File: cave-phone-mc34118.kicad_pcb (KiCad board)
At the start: 2 copper layers, 98.7 x 54.2 mm, 71 parts, among them J1 Conn_01x02_Female, SW1 L-KLS7-SK02-12E12-EG7, SW2 SW_SPST, SW3 SW_SPST, T1 SM-LP-5001, U1 LT1935, U2 MC34118, U3 MC34119G-SO8

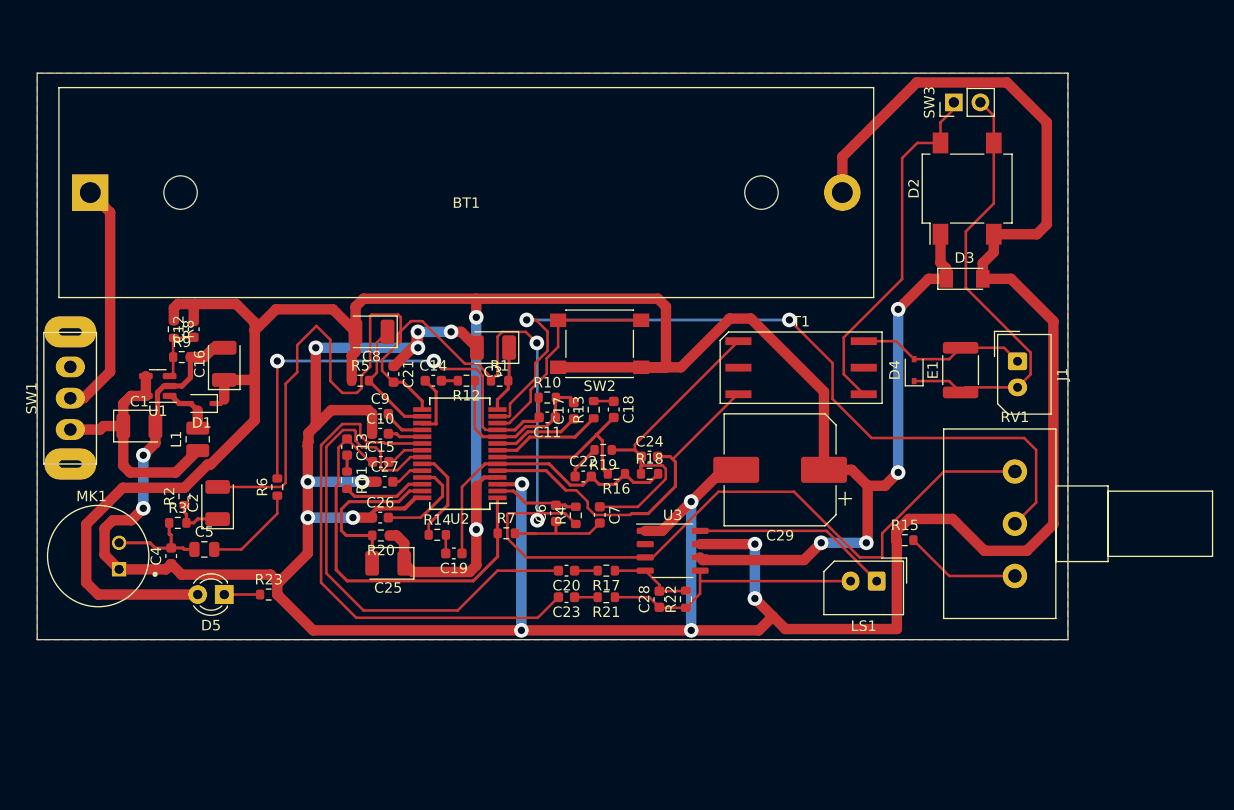
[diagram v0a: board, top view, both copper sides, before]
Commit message: Rework PCB for right MC34118 package
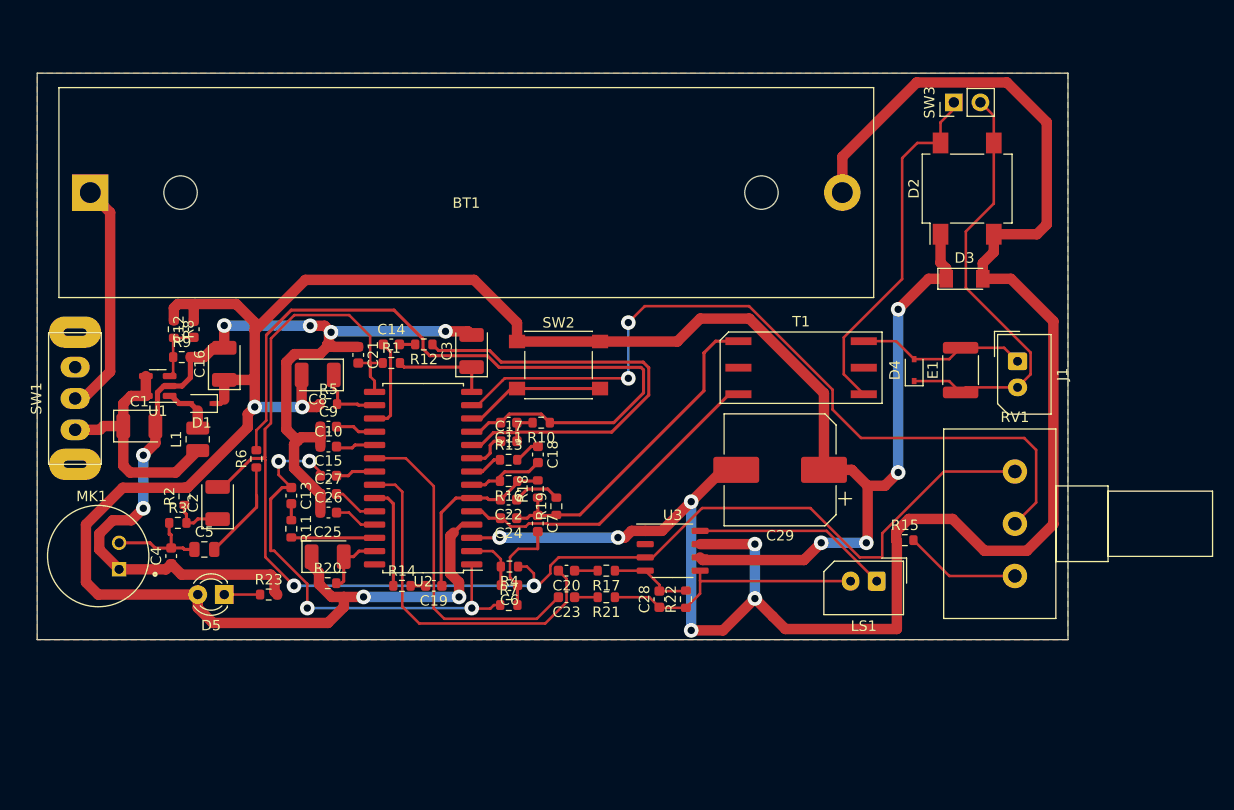
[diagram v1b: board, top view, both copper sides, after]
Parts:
- U2: footprint Package_SO:SSOP-28_5.3x10.2mm_P0.65mm -> Package_SO:SOIC-28W_7.5x17.9mm_P1.27mm
- moved C24 14.7 mm to (95.9, 112.5), turned to 180 degrees
- moved R18 10.8 mm to (98.7, 109.7), turned to 90 degrees
- moved R1 10.5 mm to (84.7, 97.6)
- moved R16 10.3 mm to (95.9, 108.9)
- moved R13 9.46 mm to (95.9, 106.9), turned to 0 degrees
- moved C18 8.44 mm to (98.7, 106.4)
- moved C6 8.18 mm to (96.0, 118.9), turned to 180 degrees
- moved R4 8.02 mm to (96.0, 117.1), turned to 180 degrees
- moved C22 7.48 mm to (95.9, 110.7), turned to 180 degrees
- moved C13 7.08 mm to (75.1, 110.3)
- moved R11 7.08 mm to (75.1, 113.5)
- moved R19 7.01 mm to (100.5, 111.3), turned to 90 degrees
- moved R7 6.87 mm to (95.9, 120.8)
- moved C17 6.87 mm to (96.0, 105.1), turned to 0 degrees
- moved R20 6.84 mm to (78.6, 118.7), turned to 0 degrees
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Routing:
- net GND: track 337.0 -> 278.8 mm, vias 16 -> 12
- net Net-(C11-Pad1): track 17.3 -> 46.4 mm
- net VB: track 161.9 -> 133.0 mm
- net Net-(C11-Pad2): track 44.3 -> 72.3 mm, vias 2 -> 0
- net Net-(C23-Pad2): track 50.0 -> 31.7 mm
- net Net-(C20-Pad2): track 50.8 -> 34.5 mm
- net VCC: track 258.6 -> 244.1 mm, vias 6 -> 8
- net Net-(C19-Pad1): track 28.7 -> 17.8 mm
- net Net-(C25-Pad2): track 16.3 -> 6.31 mm
- net Net-(C18-Pad2): track 16.9 -> 7.47 mm
- net Net-(SW2-Pad2): track 20.9 -> 13.5 mm
- net Net-(R13-Pad1): track 10.5 -> 3.17 mm
- net Net-(C13-Pad1): track 38.8 -> 45.1 mm, vias 0 -> 4
- net Net-(C8-Pad1): track 11.9 -> 6.60 mm
- net Net-(C26-Pad2): track 9.34 -> 4.12 mm
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
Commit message: WiP: New PCB (0805 SMDs)
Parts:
- removed C16: 20µF, Capacitor_Tantalum_SMD:CP_EIA-3528-21_Kemet-B
- removed D1: BAT760.115, Diode_SMD:D_SOD-323
- removed L1: 1,8µH, Inductor_SMD:L_1008_2520Metric
- removed U1: LT1935, Package_TO_SOT_SMD:SOT-23-5
- added SW4: SW_SPST, Button_Switch_SMD:SW_Push_1P1T_NO_6x6mm_H9.5mm, F.Cu at (81.8, 135.1)
- C1: value 4,7µF -> 0,1µF; footprint Capacitor_Tantalum_SMD:CP_EIA-3528-21_Kemet-B -> Capacitor_SMD:C_0805_2012Metric_Pad1.18x1.45mm_HandSolder
- C10, C11, C13, C14, C15, C17, C18, C19, C20, C22, C23, C24, C26, C27, C28, C4, C6, C7, C9: footprint Capacitor_SMD:C_0603_1608Metric -> Capacitor_SMD:C_0805_2012Metric_Pad1.18x1.45mm_HandSolder
- C12: value 150pF -> 0,1µF; footprint Capacitor_SMD:C_0603_1608Metric -> Capacitor_SMD:C_0805_2012Metric_Pad1.18x1.45mm_HandSolder
- C2, C25, C3, C8: footprint Capacitor_Tantalum_SMD:CP_EIA-3528-21_Kemet-B -> Capacitor_Tantalum_SMD:CP_EIA-3528-21_Kemet-B_Pad1.50x2.35mm_HandSolder
- C21: value 0,1µF -> 220,0µF; footprint Capacitor_SMD:C_0603_1608Metric -> Capacitor_Tantalum_SMD:CP_EIA-3528-21_Kemet-B_Pad1.50x2.35mm_HandSolder
- C5: footprint Capacitor_SMD:C_0805_2012Metric -> Capacitor_SMD:C_0805_2012Metric_Pad1.18x1.45mm_HandSolder
- R1, R10, R11, R13, R15, R17, R2, R20, R21, R22, R23, R3, R4, R5, R6, R7: footprint Resistor_SMD:R_0603_1608Metric -> Capacitor_SMD:C_0805_2012Metric_Pad1.18x1.45mm_HandSolder
- R12, R14: value 10K -> 5,1K; footprint Resistor_SMD:R_0603_1608Metric -> Capacitor_SMD:C_0805_2012Metric_Pad1.18x1.45mm_HandSolder
- R16: value 5,1K -> 51K; footprint Resistor_SMD:R_0603_1608Metric -> Capacitor_SMD:C_0805_2012Metric_Pad1.18x1.45mm_HandSolder
- R18: value 420 -> 820; footprint Resistor_SMD:R_0603_1608Metric -> Capacitor_SMD:C_0805_2012Metric_Pad1.18x1.45mm_HandSolder
- R19: value 330 -> 300K; footprint Resistor_SMD:R_0603_1608Metric -> Capacitor_SMD:C_0805_2012Metric_Pad1.18x1.45mm_HandSolder
- R8: value 29,4K -> 20K; footprint Resistor_SMD:R_0603_1608Metric -> Capacitor_SMD:C_0805_2012Metric_Pad1.18x1.45mm_HandSolder
- R9: value 10K -> 36K; footprint Resistor_SMD:R_0603_1608Metric -> Capacitor_SMD:C_0805_2012Metric_Pad1.18x1.45mm_HandSolder
- SW3: value SW_SPST -> L-KLS7-SK02-12E12-EG7; footprint Connector_PinHeader_2.54mm:PinHeader_1x02_P2.54mm_Vertical -> cave-phone:KLS7-SK02-12E12
- moved R20 1.47 mm to (78.5, 120.1)
- moved C25 0.94 mm to (78.0, 116.8)
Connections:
- C1 pad 1: Net-(C1-Pad1) -> VCC
- C12 pad 2: VCC -> Net-(C12-Pad2)
- C21 pad 1: GND -> VB
- C21 pad 2: VB -> GND
- C8 pad 1: Net-(C8-Pad1) -> VCC
- C8 pad 2: VCC -> Net-(C8-Pad2)
- D2 pad 1: VCC -> /LINE_POWER
- D2 pad 3: Net-(D2-Pad3) -> Net-(C12-Pad1)
- D2 pad 4: Net-(D2-Pad4) -> Net-(C12-Pad2)
- D3 pad 1: VCC -> /LINE_POWER
- D4 pad 1: Net-(D2-Pad3) -> Net-(C12-Pad1)
- E1 pad 1: Net-(D2-Pad3) -> Net-(C12-Pad1)
- J1 pad 2: Net-(D2-Pad3) -> Net-(C12-Pad1)
- R5 pad 2: Net-(C8-Pad1) -> Net-(C8-Pad2)
- R8 pad 1: VCC -> Net-(R8-Pad1)
- R8 pad 2: Net-(C12-Pad1) -> VCC
- R9 pad 1: Net-(C12-Pad1) -> Net-(R9-Pad1)
- R9 pad 2: GND -> Net-(C18-Pad1)
- RV1 pad 1: Net-(R15-Pad2) -> VB
- RV1 pad 3: VB -> Net-(R15-Pad2)
- SW1 pad 1: unconnected-(SW1-Pad1) -> Net-(BT1-Pad1)
- SW1 pad 2: Net-(BT1-Pad1) -> Net-(SW1-Pad2)
- SW1 pad 3: Net-(C1-Pad1) -> /LINE_POWER
- SW2 pad 1: VCC -> GND
- SW2 pad 2: Net-(SW2-Pad2) -> Net-(R8-Pad1)
- SW3 pad 1: Net-(D2-Pad4) -> unconnected-(SW3-Pad1)
- SW3 pad 2: Net-(D2-Pad3) -> Net-(SW1-Pad2)
- T1 pad 3: Net-(D2-Pad4) -> Net-(C12-Pad2)
- U2 pad 12: Net-(SW2-Pad2) -> Net-(R8-Pad1)
- U2 pad 16: Net-(C8-Pad1) -> Net-(C8-Pad2)
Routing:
- net GND: track 278.8 -> 0.00 mm, vias 12 -> 0
- net VCC: track 244.1 -> 0.00 mm, vias 8 -> 0
- net VB: track 133.0 -> 0.00 mm, vias 2 -> 0
- net Net-(RV1-Pad2): track 75.8 -> 0.00 mm, vias 2 -> 0
- net Net-(C11-Pad2): track 72.3 -> 0.00 mm
- net Net-(C11-Pad1): track 46.4 -> 0.00 mm
- net Net-(C13-Pad1): track 45.1 -> 0.00 mm, vias 4 -> 0
- net Net-(D2-Pad3): track 42.6 -> 0.00 mm
- net Net-(C20-Pad2): track 34.5 -> 0.00 mm
- net Net-(D2-Pad4): track 34.4 -> 0.00 mm
- net Net-(C24-Pad1): track 32.1 -> 0.00 mm
- net Net-(C23-Pad2): track 31.7 -> 0.00 mm
- net Net-(C24-Pad2): track 31.4 -> 0.00 mm
- net Net-(C28-Pad1): track 25.8 -> 0.00 mm
- net Net-(C1-Pad1): track 23.3 -> 0.00 mm
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- removed copper zone on F.Cu, net GND

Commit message: WiP: New PCB
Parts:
- BT1, D5, LS1, MK1, RV1: moved to B.Cu
- C10, C26, C27, C9: value 2µF -> 2,2µF
- C13, C22, C23: value 0,05µF -> 0,047µF
- C2: value 20µF -> 22µF; footprint Capacitor_Tantalum_SMD:CP_EIA-3528-21_Kemet-B_Pad1.50x2.35mm_HandSolder -> Capacitor_SMD:C_0805_2012Metric_Pad1.18x1.45mm_HandSolder
- C21: footprint Capacitor_Tantalum_SMD:CP_EIA-3528-21_Kemet-B_Pad1.50x2.35mm_HandSolder -> Capacitor_THT:CP_Radial_D8.0mm_P3.50mm; moved to B.Cu
- C25: footprint Capacitor_Tantalum_SMD:CP_EIA-3528-21_Kemet-B_Pad1.50x2.35mm_HandSolder -> Capacitor_THT:CP_Radial_D5.0mm_P2.00mm; moved to B.Cu
- C29: footprint Capacitor_SMD:CP_Elec_10x10.5 -> Capacitor_THT:CP_Radial_D10.0mm_P5.00mm; moved to B.Cu
- C3: value 5,0µF -> 4,7µF; footprint Capacitor_Tantalum_SMD:CP_EIA-3528-21_Kemet-B_Pad1.50x2.35mm_HandSolder -> Capacitor_SMD:C_0805_2012Metric_Pad1.18x1.45mm_HandSolder
- C4: value 0,02µF -> 0,022µF
- C5: value 0,2µF -> 0,22µF
- J1: footprint Connector_Molex:Molex_SPOX_5267-02A_1x02_P2.50mm_Vertical -> TerminalBlock_Phoenix:TerminalBlock_Phoenix_PT-1,5-2-5.0-H_1x02_P5.00mm_Horizontal; moved to B.Cu
- R1, R10, R11, R12, R13, R14, R15, R16, R17, R18, R19, R2, R20, R21, R22, R3, R4, R5, R6, R7, R8, R9: footprint Capacitor_SMD:C_0805_2012Metric_Pad1.18x1.45mm_HandSolder -> Resistor_SMD:R_0805_2012Metric_Pad1.20x1.40mm_HandSolder
- R23: value 5K -> 5,1K; footprint Capacitor_SMD:C_0805_2012Metric_Pad1.18x1.45mm_HandSolder -> Resistor_SMD:R_0805_2012Metric_Pad1.20x1.40mm_HandSolder
- SW1: value L-KLS7-SK02-12E12-EG7 -> L-KLS7-SS06-12F49EG7
- SW2, SW4: footprint Button_Switch_SMD:SW_Push_1P1T_NO_6x6mm_H9.5mm -> Button_Switch_THT:SW_PUSH_6mm_H5mm; moved to B.Cu
- moved SW3 83.9 mm to (54.9, 78.3)
- moved R8 59.6 mm to (123.2, 99.7), turned to 180 degrees
- moved C12 59.3 mm to (122.6, 77.1)
- moved SW4 54.8 mm to (125.5, 102.1), turned to 180 degrees
- moved R9 41.7 mm to (104.3, 84.2), turned to 180 degrees
- moved D3 34.9 mm to (107.4, 76.2), turned to -90 degrees
- moved R23 34.3 mm to (58.6, 88.6), turned to 90 degrees
- moved D5 32.8 mm to (55.7, 89.7)
- moved SW2 30.2 mm to (129.6, 106.6)
- moved C1 29.4 mm to (89.5, 98.3), turned to 180 degrees
- moved C29 28.6 mm to (96.4, 94.9), turned to 0 degrees
- moved LS1 27.4 mm to (119.6, 93.6), turned to -90 degrees
- moved D2 25.3 mm to (114.8, 77.0), turned to 0 degrees
- moved J1 24.5 mm to (146.7, 73.0)
- moved C7 23.6 mm to (106.8, 90.8)
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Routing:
- net GND: track 0.00 -> 333.5 mm, vias 0 -> 6
- net VCC: track 0.00 -> 183.1 mm, vias 0 -> 10
- net VB: track 0.00 -> 155.2 mm, vias 0 -> 2
- net Net-(RV1-Pad2): track 0.00 -> 112.3 mm
- net Net-(C11-Pad2): track 0.00 -> 70.2 mm, vias 0 -> 2
- net Net-(C24-Pad2): track 0.00 -> 61.7 mm, vias 0 -> 2
- net Net-(R8-Pad1): track 0.00 -> 61.4 mm, vias 0 -> 2
- net /LINE_POWER: track 0.00 -> 53.0 mm
- net Net-(D4-Pad2): track 0.00 -> 51.1 mm
- net Net-(C13-Pad1): track 0.00 -> 43.2 mm, vias 0 -> 2
- net Net-(R9-Pad1): track 0.00 -> 41.5 mm, vias 0 -> 2
- net Net-(C23-Pad2): track 0.00 -> 40.5 mm
- net Net-(C12-Pad1): track 0.00 -> 30.6 mm
- net Net-(C12-Pad2): track 0.00 -> 29.3 mm
- net Net-(C20-Pad2): track 0.00 -> 28.2 mm, vias 0 -> 2
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- added copper zone on F.Cu, net GND
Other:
- board size 98.7 x 54.2 mm -> 100.1 x 39.5 mm
